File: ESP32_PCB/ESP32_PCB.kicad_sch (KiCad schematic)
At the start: 27 parts, among them J1 USB_C_Receptacle, J2 ESC1, J3 ESC2, J4 Conn_02x04_Counter_Clockwise, J5 LED, U2 H3LIS331DL, U3 AP2112K-3.3, U5 ESP32-S3-MINI-1U

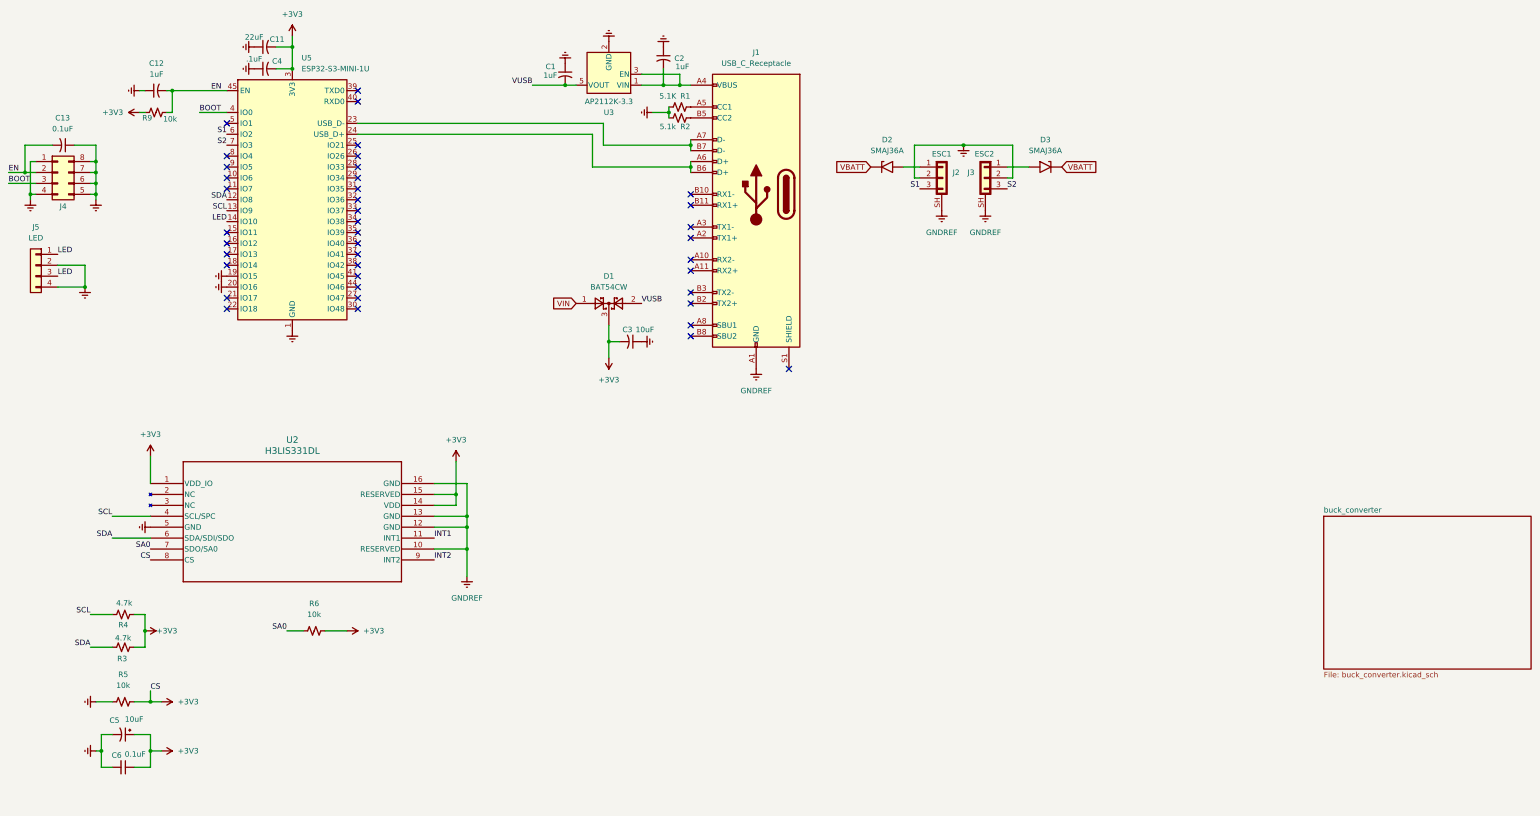
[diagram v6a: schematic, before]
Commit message: Add notes on schematics
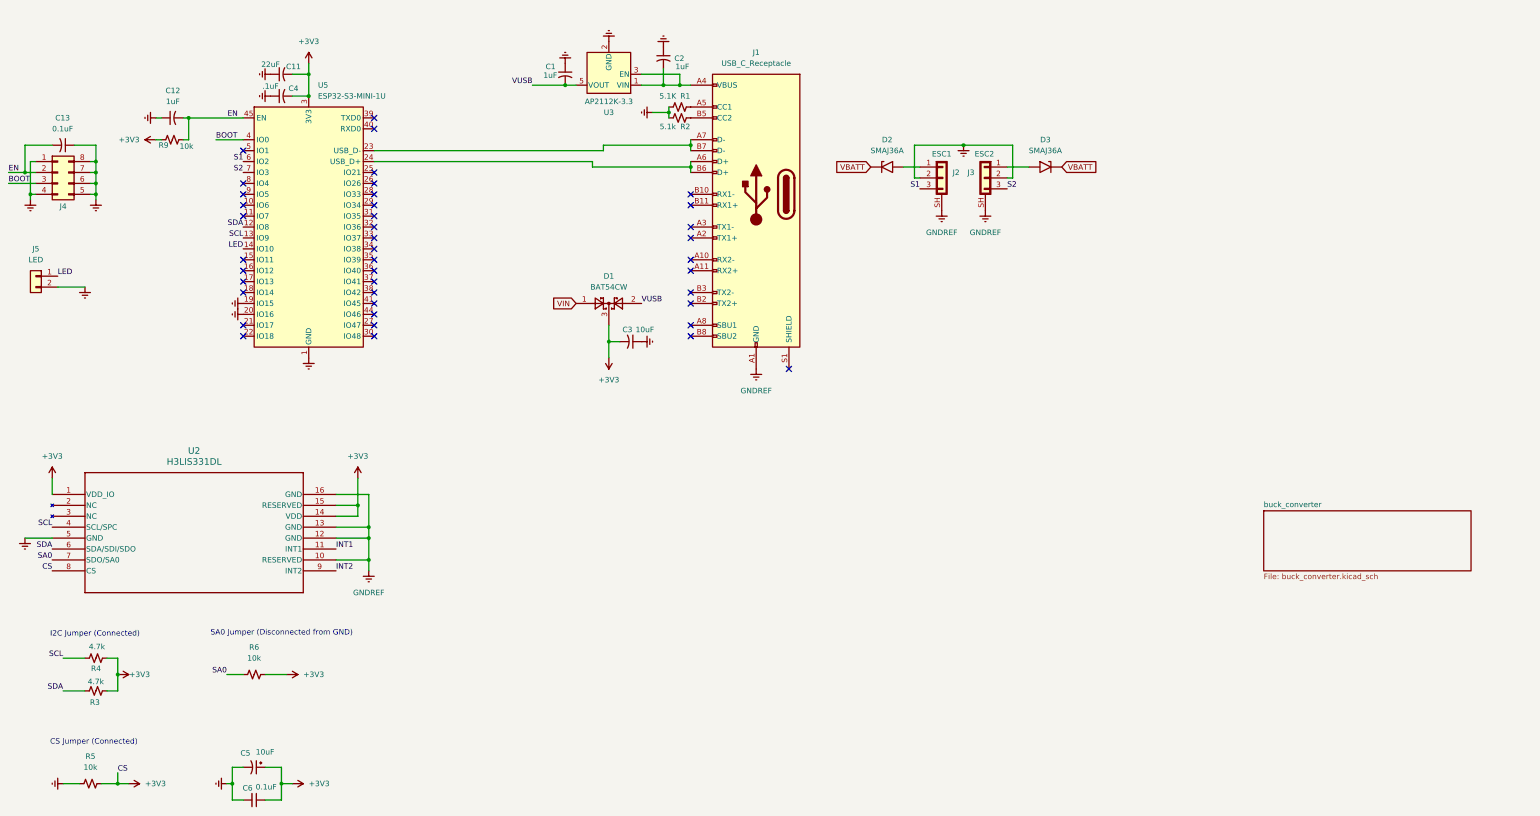
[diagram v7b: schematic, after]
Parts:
- removed J5: LED, ESC_Connectors:4_Pin, symbol Connector_Generic:Conn_01x04
- added J5: LED, symbol Connector_Generic:Conn_01x02
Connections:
- net GNDREF: now also J5.2 (Pin_2)
- net LED: now also J5.1 (Pin_1)
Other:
- note added: "CS Jumper (Connected)"
- note added: "I2C Jumper (Connected)"
- note added: "SA0 Jumper (Disconnected from GND)"
- moved on the sheet: C11, C12, C4, C5, C6, R3, R4, R5, R6, R9, U2, U5
